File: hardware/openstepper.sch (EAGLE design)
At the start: 1 part

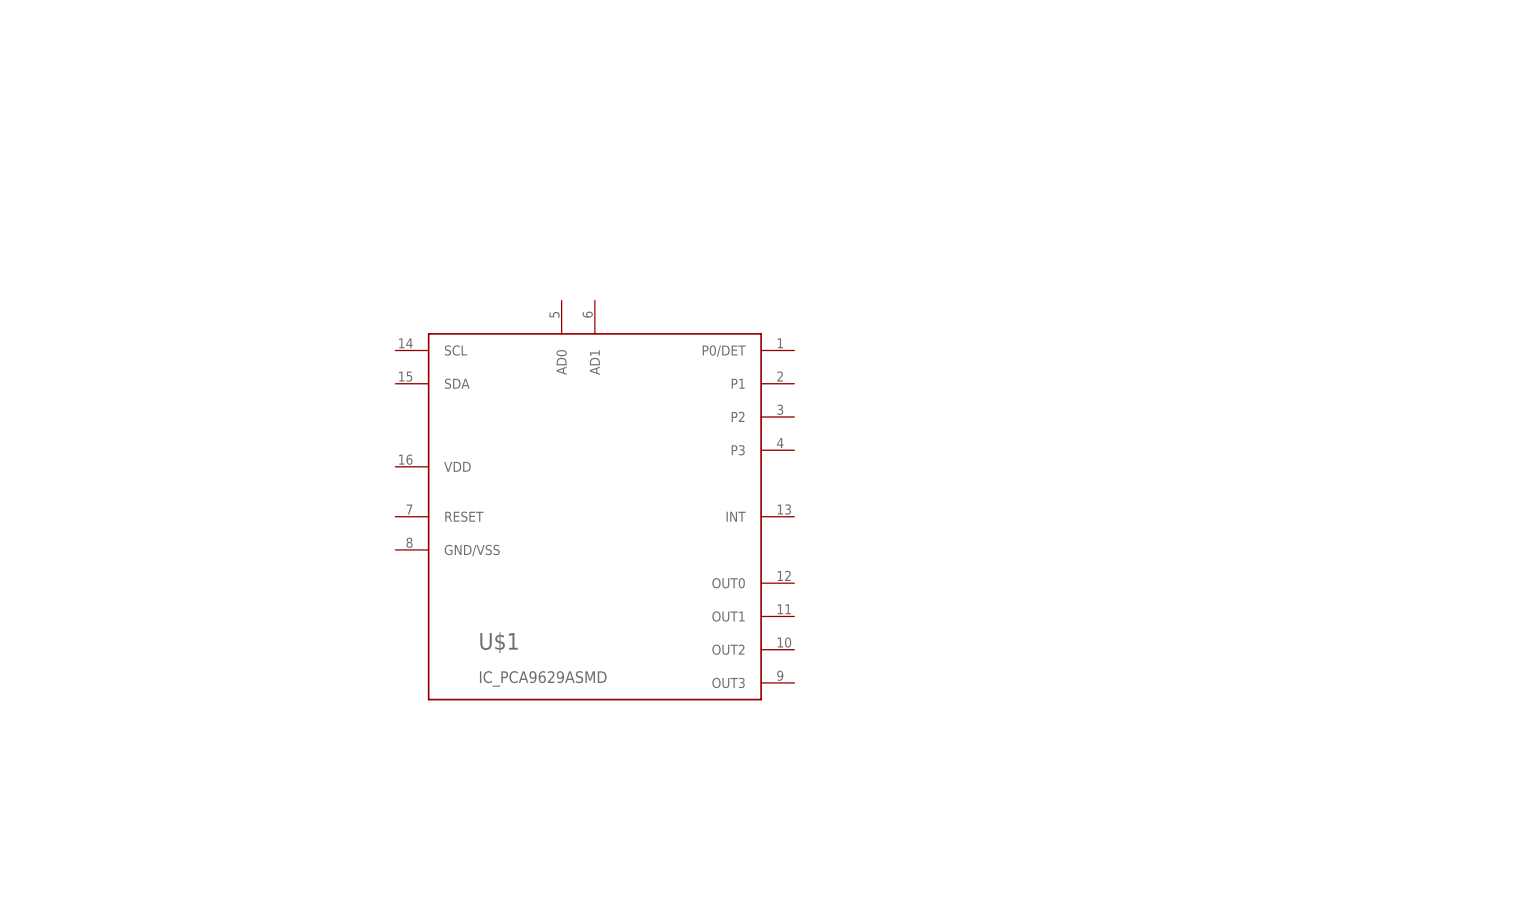
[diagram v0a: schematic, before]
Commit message: schema with darlington array  and controller
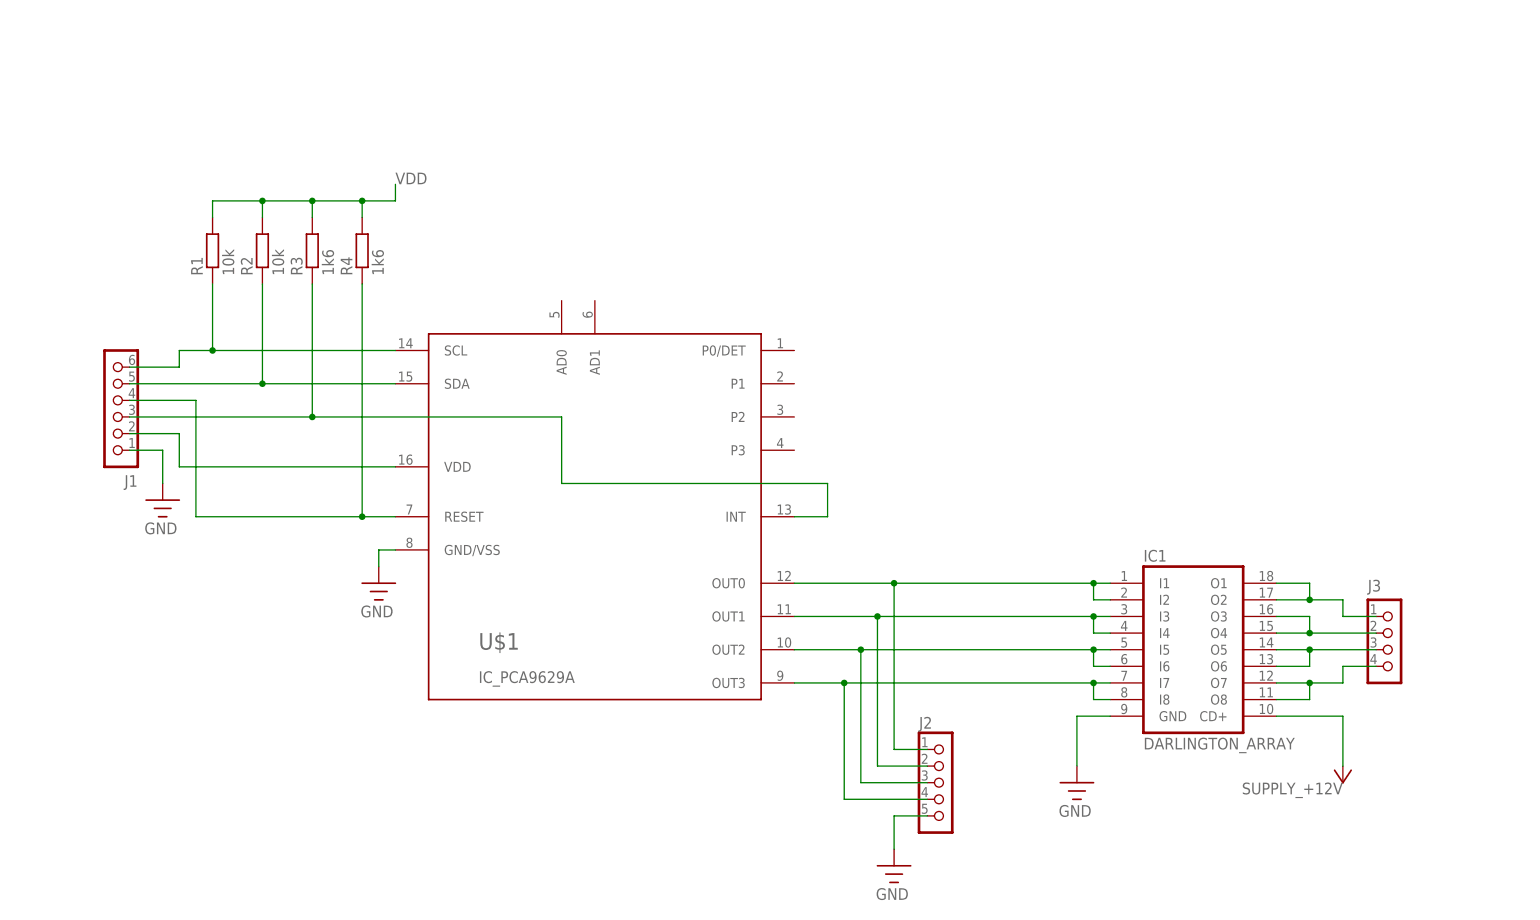
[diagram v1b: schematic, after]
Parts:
- added IC1: DARLINGTON_ARRAY, openstepper:IC_ULN2803A-SO-18
- added J1: CON_HEADER_1X06-PTH, dp_devices:CON_HEADER_1X06-PTH
- added J2: CON_HEADER_1X05-PTH, dp_devices:CON_HEADER_1X05-PTH
- added J3: CON_HEADER_1X04, dp_devices:CON_HEADER_1X04
- added R1, R2: 10k, dp_devices:RESISTOR-1206
- added R3, R4: 1k6, dp_devices:RESISTOR-1206
- U$1: value IC_PCA9629ASMD -> IC_PCA9629A; device openstepper:IC_PCA9629ASMD -> openstepper:IC_PCA9629A
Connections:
- new net +12V: IC1.CD+
- new net GND: IC1.GND, J1.1, J2.5, U$1.GND/VSS
- new net INIT: J1.3, R3.1, U$1.INT
- new net N$1: IC1.I1, IC1.I2, J2.1, U$1.OUT0
- new net N$10: IC1.O7, IC1.O8, J3.4
- new net N$11: J1.4, R4.1, U$1.RESET
- new net N$12: J1.2, U$1.VDD
- new net N$2: IC1.I3, IC1.I4, J2.2, U$1.OUT1
- new net N$3: IC1.I5, IC1.I6, J2.3, U$1.OUT2
- new net N$4: IC1.I7, IC1.I8, J2.4, U$1.OUT3
- new net N$5: J1.6, R1.1, U$1.SCL
- new net N$6: IC1.O1, IC1.O2, J3.1
- new net N$7: J1.5, U$1.SDA
- new net N$8: IC1.O3, IC1.O4, J3.2
- new net N$9: IC1.O5, IC1.O6, J3.3
- new net VDD: R1.2, R2.2, R3.2, R4.2

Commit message: change symbol in lib, schema updated
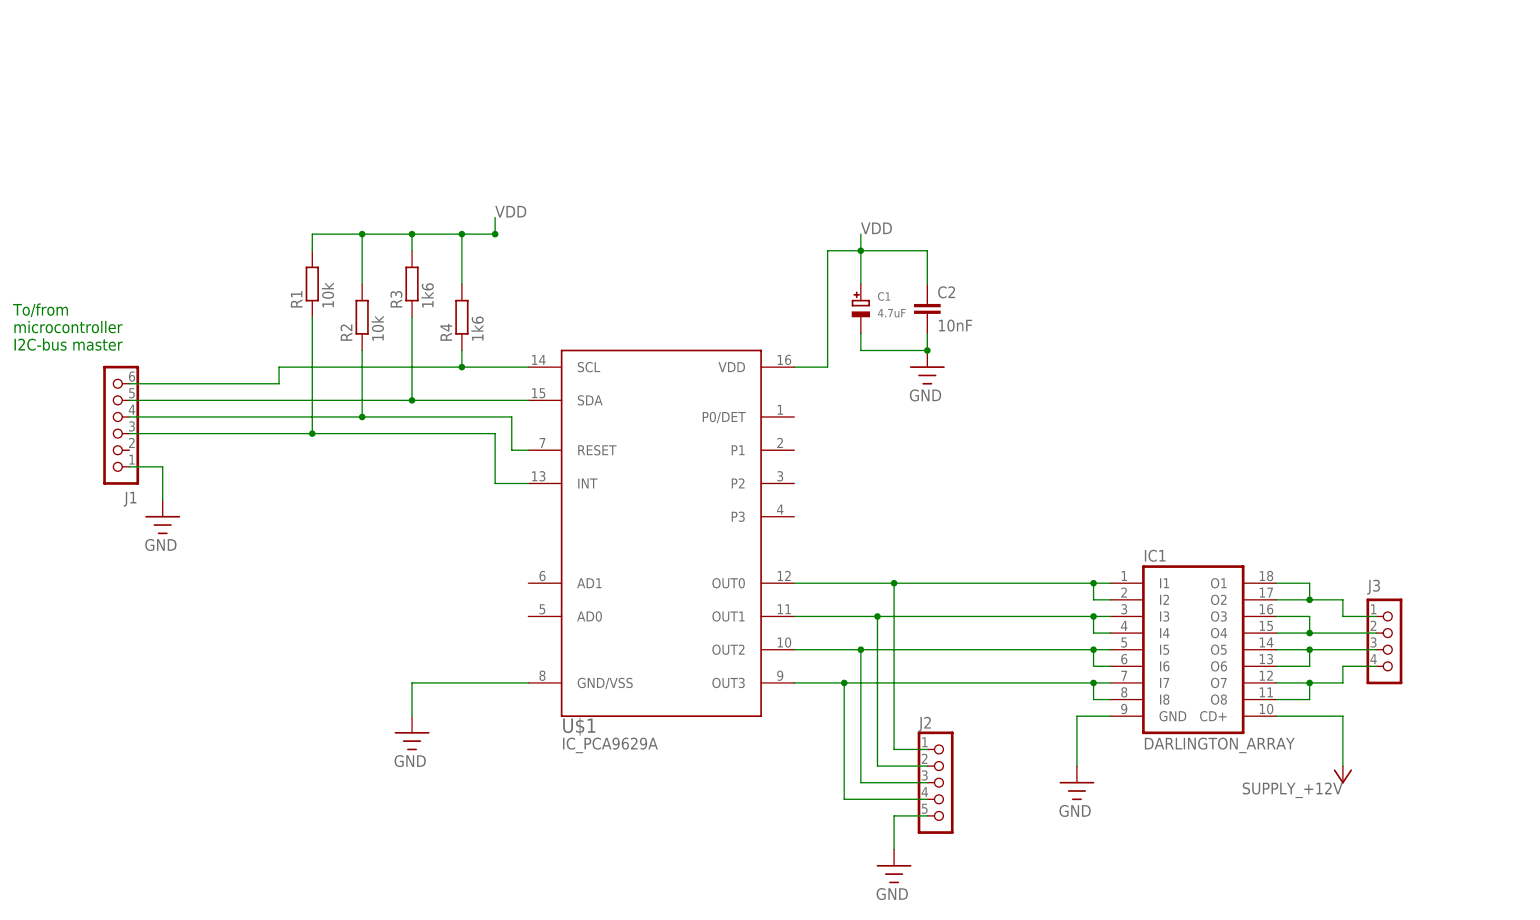
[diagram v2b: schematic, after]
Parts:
- added C1: 4.7uF, microbuilder:CAP_TANTALUMC/6032_REFLOW
- added C2: 10nF, SparkFun-Capacitors:10NF-CER
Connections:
- removed net N$11: J1.4, R4.1, U$1.RESET
- removed net N$12: J1.2, U$1.VDD
- new net N$14: J1.4, R2.1, U$1.RESET
- net GND: now also C1.-, C2.2
- net INIT: now also R1.1; no longer R3.1
- net N$5: now also R4.1; no longer R1.1
- net N$7: now also R3.1
- net VDD: now also C1.+, C2.1, U$1.VDD
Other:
- note added: "To/from microcontroller I2C-bus master"
- moved on the sheet: J1, R1, R2, R3, R4, U$1

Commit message: schema update + datasheets
missing power regulator and optocopler setup (change to PC817)
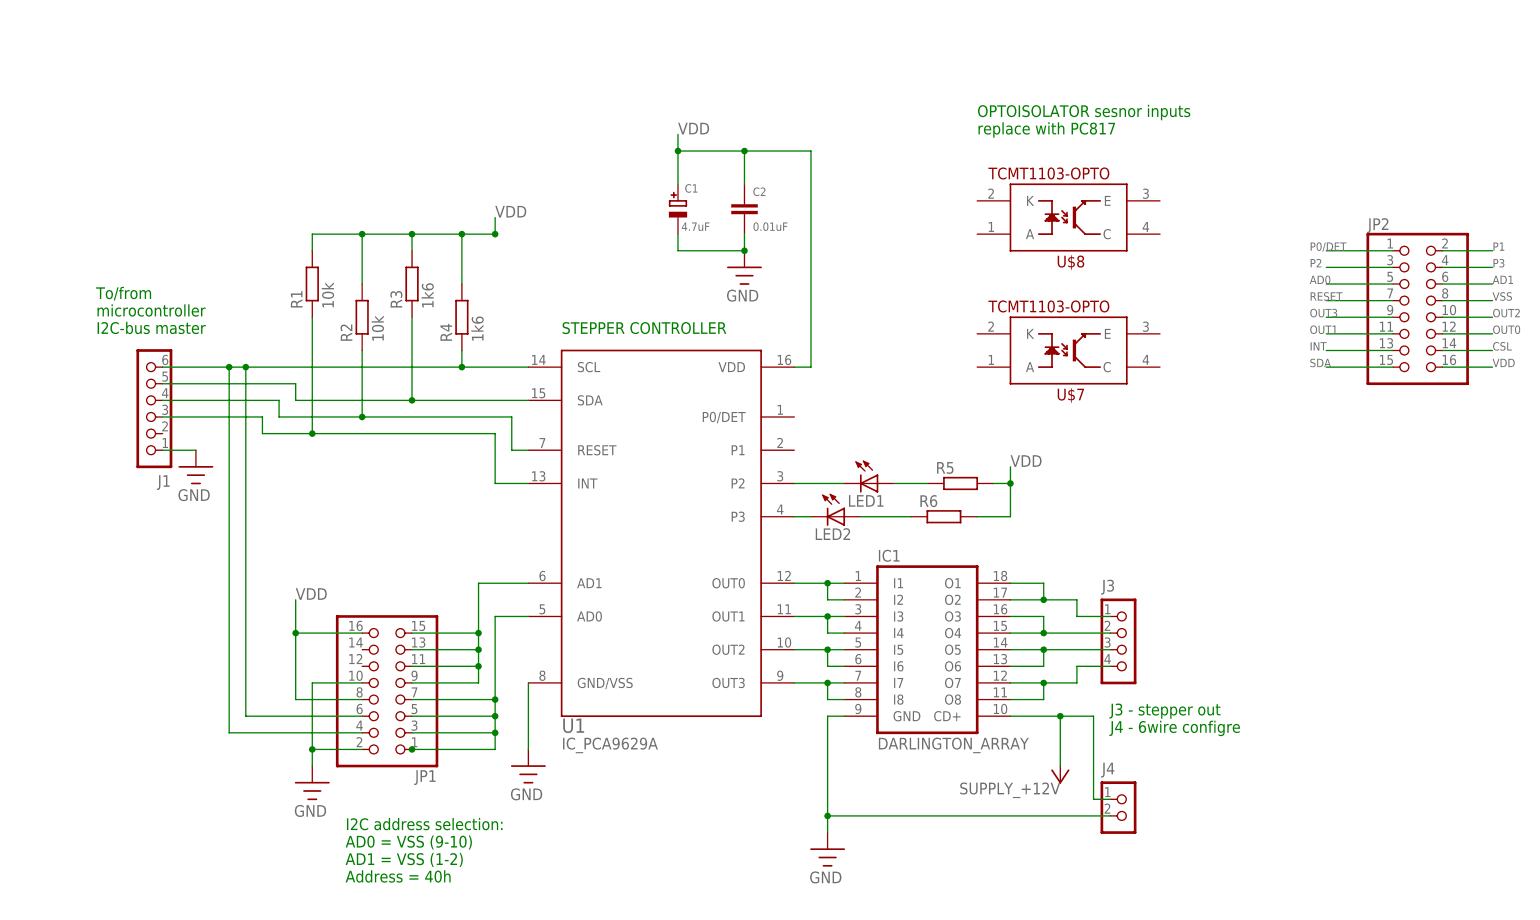
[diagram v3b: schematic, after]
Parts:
- removed J2: CON_HEADER_1X05-PTH, dp_devices:CON_HEADER_1X05-PTH
- added J4: CON_HEADER_1X02-PTH, dp_devices:CON_HEADER_1X02-PTH
- added JP1, JP2: (no value), microbuilder:HEADER-2X8
- added LED1, LED2: (no value), dp_devices:LED-0805
- added R5, R6: (no value), dp_devices:RESISTORR805-0805
- added U$7, U$8: TCMT1103-OPTO, SparkFun-DiscreteSemi:TCMT1103-OPTO
- C1: device microbuilder:CAP_TANTALUMC/6032_REFLOW -> microbuilder:CAP_ELECTROLYTICPANASONIC_C
- C2: value 10nF -> 0.01uF; device SparkFun-Capacitors:10NF-CER -> dp_devices:CAPACITOR_NPOL-0805
- renumbered U$1 to U1
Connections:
- new net AD0: JP2.5
- new net AD1: JP2.6
- new net CSL: JP2.14
- new net INT: JP2.13
- new net N$11: LED1.A, R5.1
- new net N$12: LED2.C, U1.P3
- new net N$13: LED1.C, U1.P2
- new net N$15: LED2.A, R6.1
- new net N$16: JP1.1, JP1.3, JP1.5, JP1.7, U1.AD0
- new net N$17: JP1.11, JP1.13, JP1.15, JP1.9, U1.AD1
- new net OUT0: JP2.12
- new net OUT1: JP2.11
- new net OUT2: JP2.10
- new net OUT3: JP2.9
- new net P0/DET: JP2.1
- new net P1: JP2.2
- new net P2: JP2.3
- new net P3: JP2.4
- new net RESET: JP2.7
- new net SDA: JP2.15
- new net VSS: JP2.8
- net +12V: now also J4.1
- net GND: now also J4.2, JP1.10, JP1.2; no longer J2.5
- net N$1: no longer J2.1
- net N$2: no longer J2.2
- net N$3: no longer J2.3
- net N$4: no longer J2.4
- net N$5: now also JP1.4, JP1.6
- net VDD: now also JP1.16, JP1.8, JP2.16, R5.2, R6.2
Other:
- note added: "I2C address selection: AD0 = VSS (9-10) AD1 = VSS (1-2) Address = 40h"
- note added: "J3 - stepper out J4 - 6wire configre"
- note added: "OPTOISOLATOR sesnor inputs replace with PC817"
- note added: "STEPPER CONTROLLER"
- moved on the sheet: C1, IC1, J1, J3

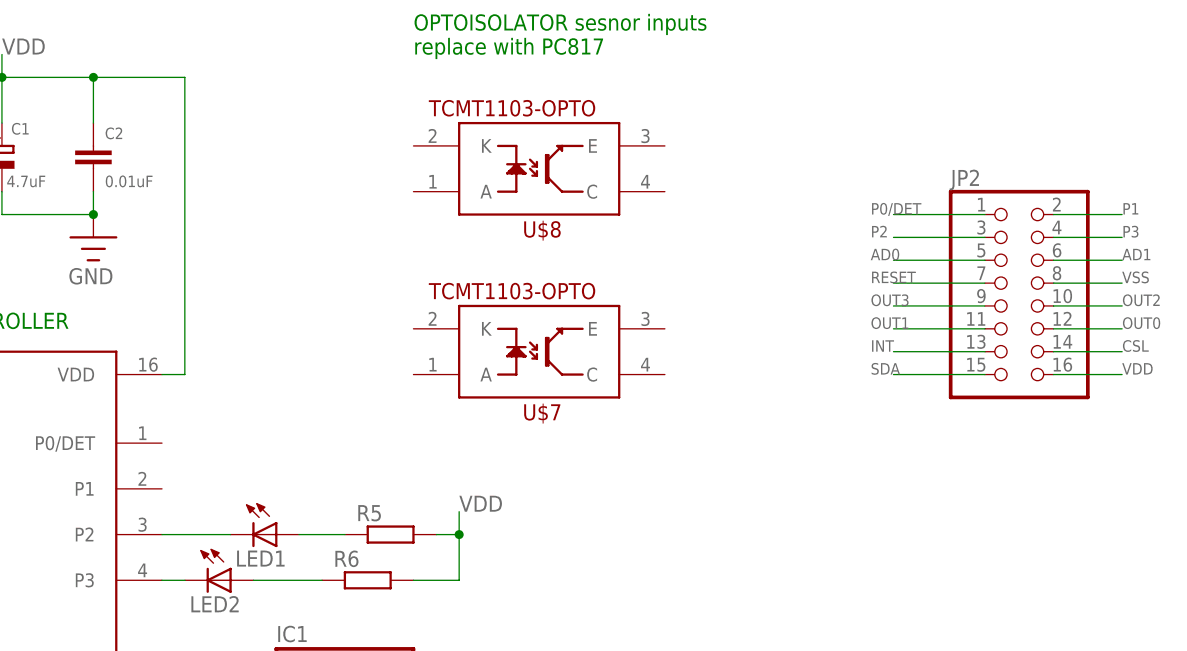
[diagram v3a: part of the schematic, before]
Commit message: rough board layout
and split breakout into two parts, also fixed names and labels on
breakout
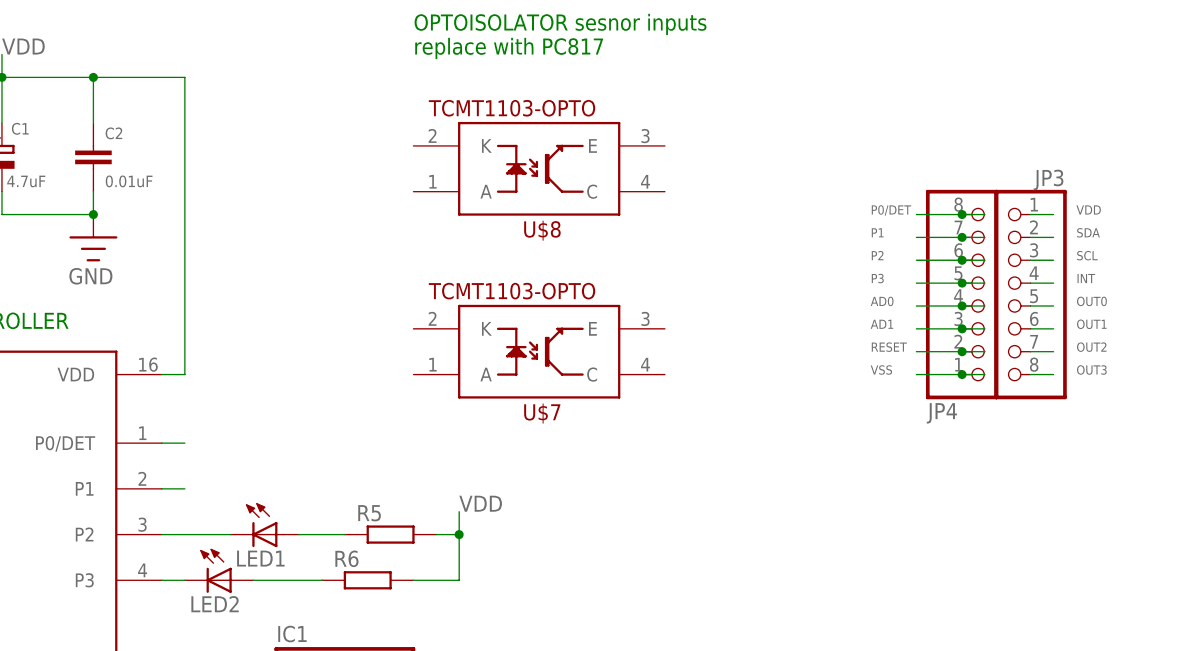
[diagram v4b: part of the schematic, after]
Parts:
- removed JP2: (no value), microbuilder:HEADER-2X8
- added JP3, JP4: (no value), adafruit:PINHD-1X8BIG
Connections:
- removed net CSL: JP2.14
- removed net INIT: J1.3, R1.1, U1.INT
- removed net N$1: IC1.I1, IC1.I2, U1.OUT0
- removed net N$12: LED2.C, U1.P3
- removed net N$13: LED1.C, U1.P2
- removed net N$14: J1.4, R2.1, U1.RESET
- removed net N$16: JP1.1, JP1.3, JP1.5, JP1.7, U1.AD0
- removed net N$17: JP1.11, JP1.13, JP1.15, JP1.9, U1.AD1
- removed net N$2: IC1.I3, IC1.I4, U1.OUT1
- removed net N$3: IC1.I5, IC1.I6, U1.OUT2
- removed net N$4: IC1.I7, IC1.I8, U1.OUT3
- removed net N$5: J1.6, JP1.4, JP1.6, R4.1, U1.SCL
- removed net N$7: J1.5, R3.1, U1.SDA
- new net SCL: J1.6, JP1.4, JP1.6, JP3.3, R4.1, U1.SCL
- net AD0: now also JP1.1, JP1.3, JP1.5, JP1.7, JP4.4, U1.AD0; no longer JP2.5
- net AD1: now also JP1.11, JP1.13, JP1.15, JP1.9, JP4.3, U1.AD1; no longer JP2.6
- net INT: now also J1.3, JP3.4, R1.1, U1.INT; no longer JP2.13
- net OUT0: now also IC1.I1, IC1.I2, JP3.5, U1.OUT0; no longer JP2.12
- net OUT1: now also IC1.I3, IC1.I4, JP3.6, U1.OUT1; no longer JP2.11
- net OUT2: now also IC1.I5, IC1.I6, JP3.7, U1.OUT2; no longer JP2.10
- net OUT3: now also IC1.I7, IC1.I8, JP3.8, U1.OUT3; no longer JP2.9
- net P0/DET: now also JP4.8, U1.P0/DET; no longer JP2.1
- net P1: now also JP4.7, U1.P1; no longer JP2.2
- net P2: now also JP4.6, LED1.C, U1.P2; no longer JP2.3
- net P3: now also JP4.5, LED2.C, U1.P3; no longer JP2.4
- net RESET: now also J1.4, JP4.2, R2.1, U1.RESET; no longer JP2.7
- net SDA: now also J1.5, JP3.2, R3.1, U1.SDA; no longer JP2.15
- net VDD: now also JP3.1; no longer JP2.16
- net VSS: now also JP4.1; no longer JP2.8
